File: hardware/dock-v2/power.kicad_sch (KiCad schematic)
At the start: 31 parts, among them J101 TYPE-C-31-M-12, U101 TPD4E1U06DBVR, U102 CH224A, U103 TPS54331DR, U104 AMS1117-3.3

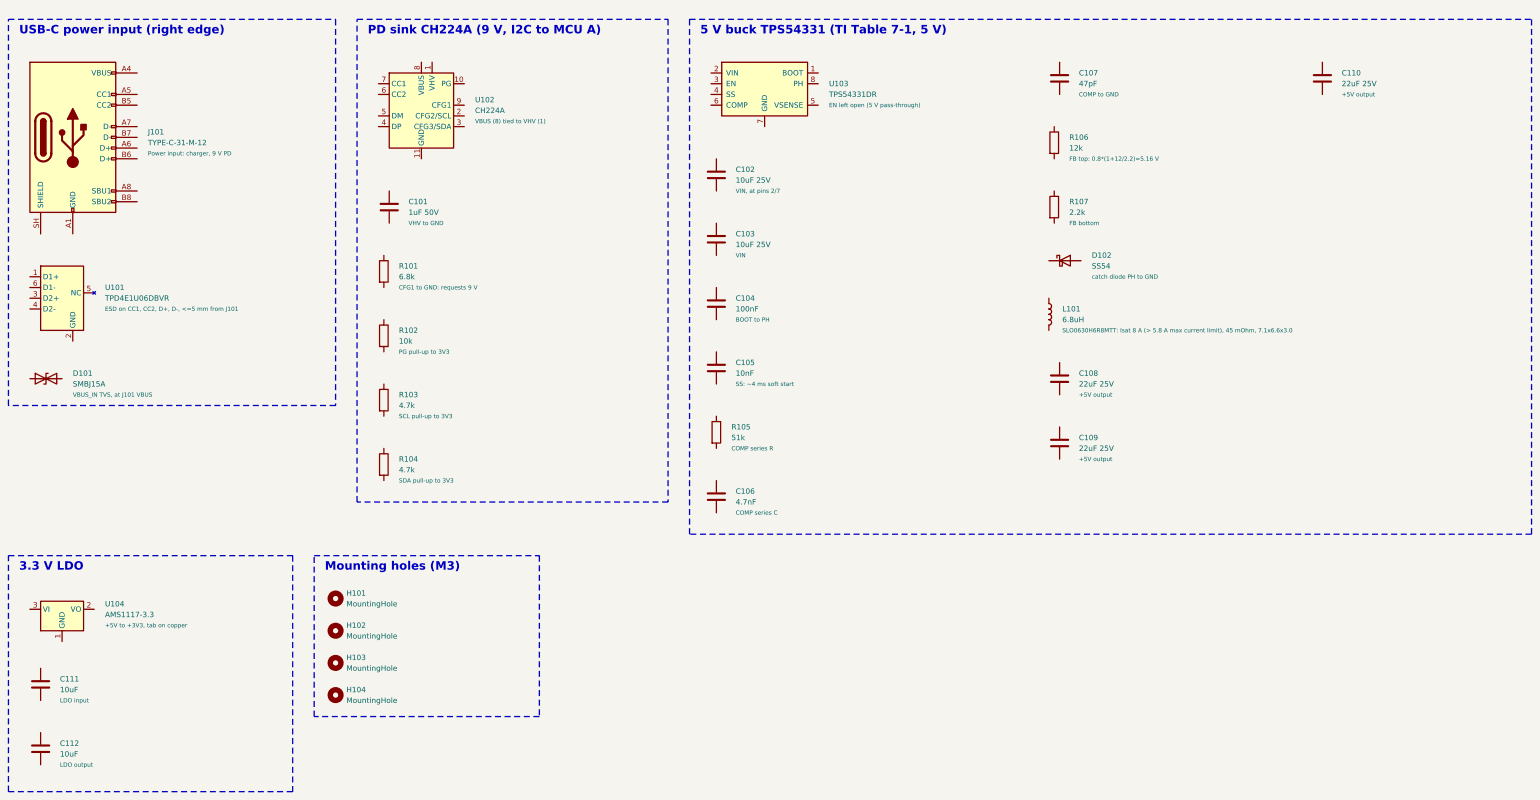
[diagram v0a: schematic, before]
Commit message: Dock v2 schematic: wiring in progress (user's work, snapshot before fixes)
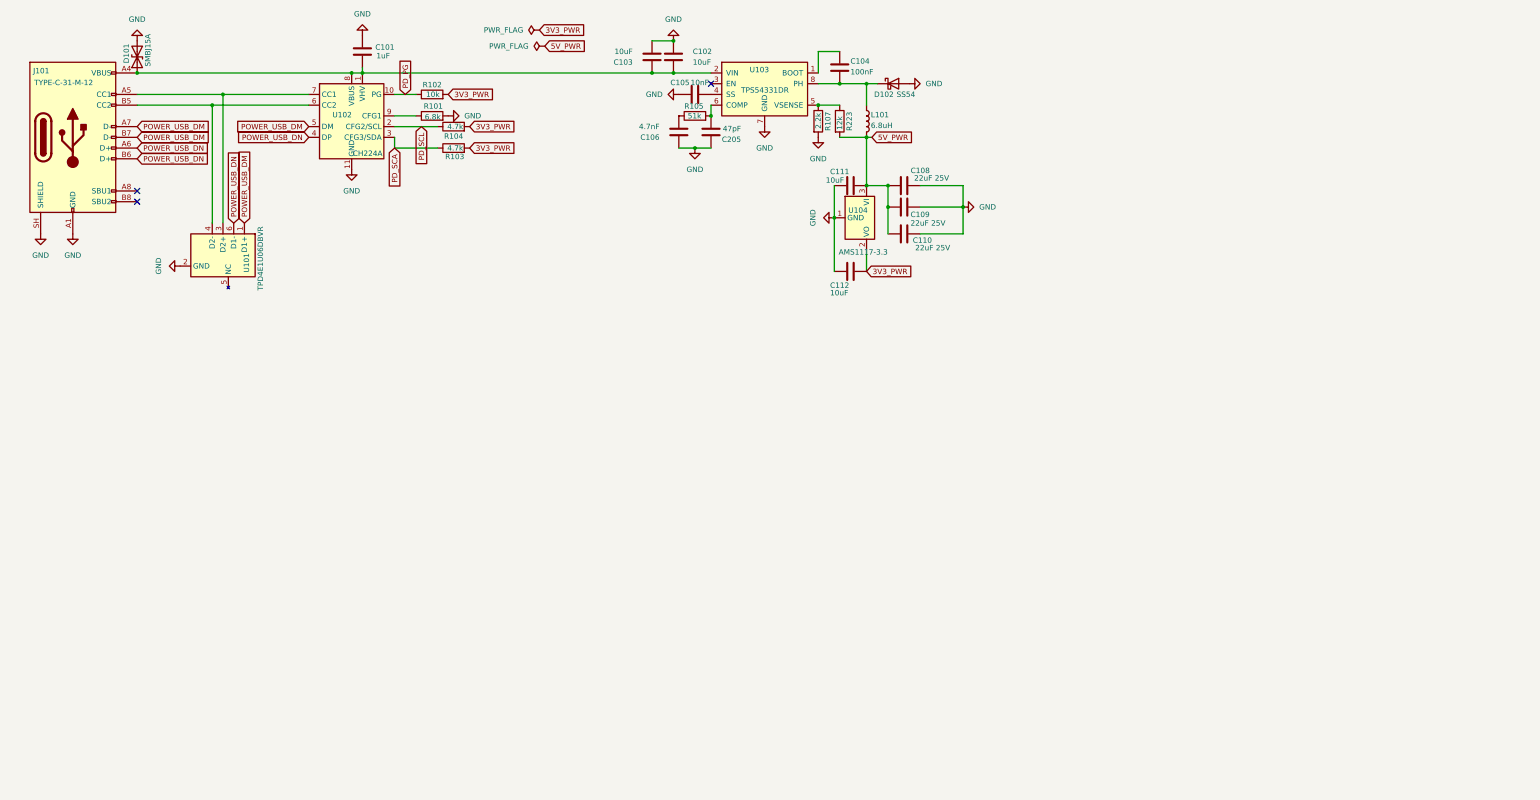
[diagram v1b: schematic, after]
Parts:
- removed C107: 47pF, Capacitor_SMD:C_0402_1005Metric, symbol Device:C
- removed H101, H102, H103, H104: MountingHole, MountingHole:MountingHole_3.2mm_M3, symbol Mechanical:MountingHole
- removed R106: 12k, Resistor_SMD:R_0402_1005Metric, symbol Device:R
- added C205: 47pF, Capacitor_SMD:C_0402_1005Metric, symbol Device:C
- added R223: 12k, Resistor_SMD:R_0402_1005Metric, symbol Device:R
- C101: value 1uF 50V -> 1uF
- C102, C103: value 10uF 25V -> 10uF
- L101: footprint Inductor_SMD:L_TechFuse_SL0630 -> (none); LCSC C207841 -> C10167; Note SLO0630H6R8MTT: Isat 8 A (> 5.8 A max current limit), 45 mO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 -> SMDRH105R-6R8NT (Ext) or a Basic 6.8 uH, 3 A+: pick footpri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
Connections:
- net PD_SCL: now reaches R104.1
- net PD_SCL: now also U102.2 (CFG2/SCL)
- net 3V3_PWR: now reaches R104.2
- net 3V3_PWR: now also C112.1, R102.2, R103.2, U104.2 (VO)
- net at C103.1: now also C101.2, C102.2, D101.1 (A1), J101.A4 (VBUS), J101.A9 (VBUS), J101.B4 (VBUS), J101.B9 (VBUS), U102.1 (VHV), U102.8 (VBUS), U103.2 (VIN)
- net GND: now reaches C103.2
- net GND: now also C101.1, C102.1, C105.1, C106.1, C108.2, C109.1, C110.2, C111.2, C112.2, D101.2 (A2), D102.2 (A), J101.A1 (GND), J101.A12 (GND), J101.B1 (GND), J101.B12 (GND), J101.SH (SHIELD), R101.2, R107.2, U101.2 (GND), U102.11 (GND), U103.7 (GND), U104.1 (GND), C205.1
- net at R105.1: now also C106.2
- net at R105.2: now also U103.6 (COMP), C205.2
- net 5V_PWR: now reaches C111.1
- net 5V_PWR: now also C108.1, C109.2, C110.1, L101.2, U104.3 (VI), R223.2
- net at D102.1 (K): now also C104.2, L101.1, U103.8 (PH)
- net at R107.1: now also U103.5 (VSENSE), R223.1
- net at J101.A5 (CC1): now also U101.3 (D2+), U102.7 (CC1)
- net POWER_USB_DN: now reaches J101.A6 (D+)
- net POWER_USB_DN: now also J101.B6 (D+), U101.6 (D1-), U102.4 (DP)
- net POWER_USB_DM: now reaches J101.A7 (D-)
- net POWER_USB_DM: now also J101.B7 (D-), U101.1 (D1+), U102.5 (DM)
- net at J101.B5 (CC2): now also U101.4 (D2-), U102.6 (CC2)
- net at R101.1: now also U102.9 (CFG1)
- net at C105.2: now also U103.4 (SS)
- net PD_PG: now reaches U102.10 (PG)
- net PD_PG: now also R102.1
- net PD_SCA: now reaches U102.3 (CFG3/SDA)
- net PD_SCA: now also R103.1
- net at C104.1: now also U103.1 (BOOT)
- no-connect marks 0 -> 3
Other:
- note removed: "3.3 V LDO"
- note removed: "5 V buck TPS54331 (TI Table 7-1, 5 V)"
- note removed: "Mounting holes (M3)"
- note removed: "PD sink CH224A (9 V, I2C to MCU A)"
- note removed: "USB-C power input (right edge)"
